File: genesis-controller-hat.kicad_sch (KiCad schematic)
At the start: 1 part, among them J1 GPIO

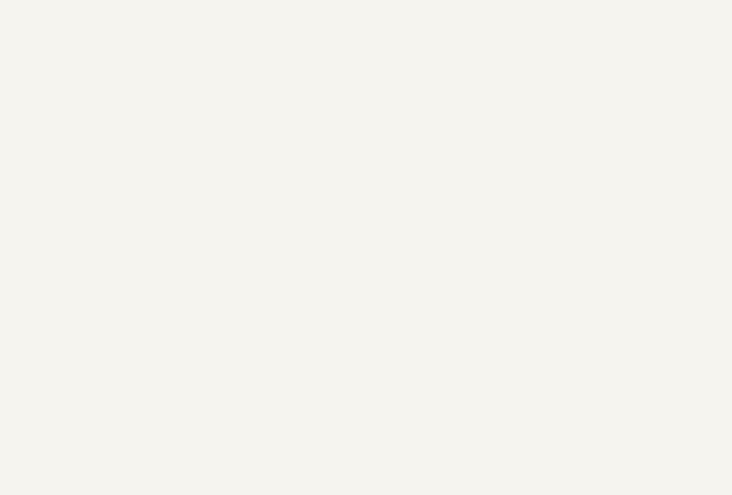
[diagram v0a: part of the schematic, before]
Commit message: Wire Player 1 DB9 connector (J2) to the GPIO header
Up/Down/Left/Right/TL/SELECT/TR land on GPIO5/6/7/9/4/10 respectively per
sega_board.h; +3.3V and GND are local power symbols that merge onto the
header's existing +3.3V/GND nets by KiCad's global-power-symbol naming
rule, and the shell/mounting pad is explicitly marked no-connect per the
approved no-extra-protection design.

Co-Authored-By: Claude Sonnet 5 <noreply@anthropic.com>
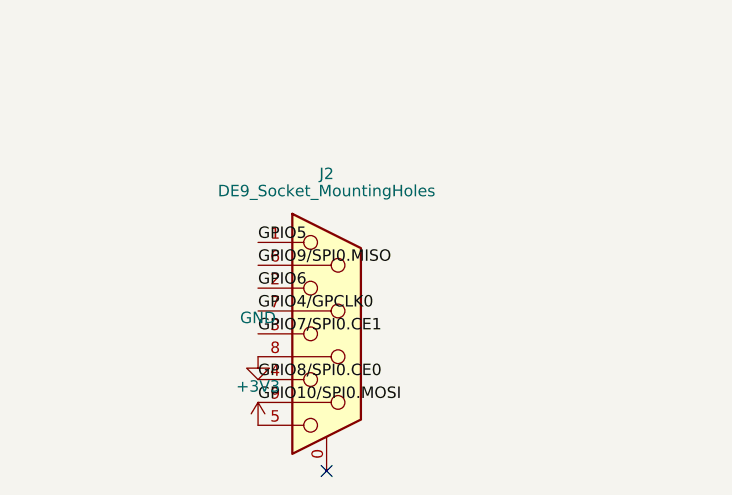
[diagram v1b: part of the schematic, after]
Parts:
- added J2: DE9_Socket_MountingHoles, Connector_Dsub:DSUB-9_Socket_Vertical_P2.77x2.84mm_MountingHoles, symbol Connector:DE9_Socket_MountingHoles
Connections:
- net +3V3: now also J2.5
- net GND: now also J2.8
- net GPIO10/SPI0.MOSI: now also J2.9
- net GPIO4/GPCLK0: now also J2.7
- net GPIO5: now also J2.1
- net GPIO6: now also J2.2
- net GPIO7/SPI0.CE1: now also J2.3
- net GPIO8/SPI0.CE0: now also J2.4
- net GPIO9/SPI0.MISO: now also J2.6
- no-connect marks 14 -> 15
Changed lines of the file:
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@@
 		(at 73.66 76.2)
 	)
+	(symbol
+		(lib_id "Connector:DE9_Socket_MountingHoles")
+		(at 50.8 254.0 0)
+		(unit 1)
+		(exclude_from_sim no)
+		(in_bom yes)
+		(on_board yes)
+		(dnp no)
+		(property "Reference" "J2"
+			(at 50.8 236.22 0)
+			(effects
+				(font
+					(size 1.27 1.27)
+				)
+			)
+		)
+		(property "Value" "DE9_Socket_MountingHoles"
+			(at 50.8 238.125 0)
+			(effects
+				(font
+					(size 1.27 1.27)
+				)
+			)
+		)
+		(property "Footprint" "Connector_Dsub:DSUB-9_Socket_Vertical_P2.77x2.84mm_MountingHoles"
+			(at 50.8 254.0 0)
+			(effects
+				(font
+					(size 1.27 1.27)
+				)
+				(hide yes)
+			)
+		)
+		(property "Datasheet" "~"
+			(at 50.8 254.0 0)
+			(effects
+				(font
+					(size 1.27 1.27)
+				)
+				(hide yes)
+			)
+		)
+		(instances
+			(project "RaspberryPi-HAT"
+				(path "/e63e39d7-6ac0-4ffd-8aa3-1841a4541b55"
+					(reference "J2")
+					(unit 1)
+				)
+			)
+		)
+	)
+	(label "GPIO5"
+		(at 43.18 243.84 180)
+		(effects
+			(font
+				(size 1.27 1.27)
+			)
+			(justify left bottom)
+		)
+	)
+	(label "GPIO6"
+		(at 43.18 248.92 180)
+		(effects
+			(font
+				(size 1.27 1.27)
+			)
+			(justify left bottom)
+		)
+	)
+	(label "GPIO7{slash}SPI0.CE1"
+		(at 43.18 254.0 180)
+		(effects
+			(font
+				(size 1.27 1.27)
+			)
+			(justify left bottom)
+		)
+	)
+	(label "GPIO8{slash}SPI0.CE0"
+		(at 43.18 259.08 180)
+		(effects
+			(font
+				(size 1.27 1.27)
+			)
+			(justify left bottom)
+		)
+	)
+	(label "GPIO9{slash}SPI0.MISO"
+		(at 43.18 246.38 180)
+		(effects
+			(font
+				(size 1.27 1.27)
+			)
+			(justify left bottom)
+		)
+	)
+	(label "GPIO4{slash}GPCLK0"
+		(at 43.18 251.46 180)
+		(effects
+			(font
+				(size 1.27 1.27)
+			)
+			(justify left bottom)
+		)
+	)
+	(label "GPIO10{slash}SPI0.MOSI"
+		(at 43.18 261.62 180)
+		(effects
+			(font
+				(size 1.27 1.27)
+			)
+			(justify left bottom)
+		)
+	)
+	(symbol
+		(lib_id "power:+3.3V")
+		(at 43.18 264.16 0)
+		(unit 1)
+		(exclude_from_sim no)
+		(in_bom yes)
+		(on_board yes)
+		(dnp no)
+		(property "Reference" "#PWR901"
+			(at 43.18 267.97 0)
+			(effects
+				(font
+					(size 1.27 1.27)
+				)
+				(hide yes)
+			)
+		)
+		(property "Value" "+3V3"
+			(at 43.18 259.84000000000003 0)
+			(effects
+				(font
+					(size 1.27 1.27)
+				)
+			)
+		)
+		(property "Footprint" ""
+			(at 43.18 264.16 0)
+			(effects
+				(font
+					(size 1.27 1.27)
+				)
+			)
+		)
+		(property "Datasheet" ""
+			(at 43.18 264.16 0)
+			(effects
+				(font
+					(size 1.27 1.27)
+				)
+			)
+		)
+		(pin "1"
+		)
+		(instances
+			(project "RaspberryPi-HAT"
+				(path "/e63e39d7-6ac0-4ffd-8aa3-1841a4541b55"
+					(reference "#PWR901")
+					(unit 1)
+				)
+			)
+		)
+	)
+	(symbol
+		(lib_id "power:GND")
+		(at 43.18 256.54 0)
+		(unit 1)
+		(exclude_from_sim no)
+		(in_bom yes)
+		(on_board yes)
+		(dnp no)
+		(property "Reference" "#PWR902"
+			(at 43.18 260.35 0)
+			(effects
+				(font
+					(size 1.27 1.27)
+				)
+				(hide yes)
+			)
+		)
+		(property "Value" "GND"
+			(at 43.18 252.22000000000003 0)
+			(effects
+				(font
+					(size 1.27 1.27)
+				)
+			)
+		)
+		(property "Footprint" ""
+			(at 43.18 256.54 0)
+			(effects
+				(font
+					(size 1.27 1.27)
+				)
+			)
+		)
+		(property "Datasheet" ""
+			(at 43.18 256.54 0)
+			(effects
+				(font
+					(size 1.27 1.27)
+				)
+			)
+		)
+		(pin "1"
+		)
+		(instances
+			(project "RaspberryPi-HAT"
+				(path "/e63e39d7-6ac0-4ffd-8aa3-1841a4541b55"
+					(reference "#PWR902")
+					(unit 1)
+				)
+			)
+		)
+	)
+	(no_connect
+		(at 50.8 269.24)
+	)
 )

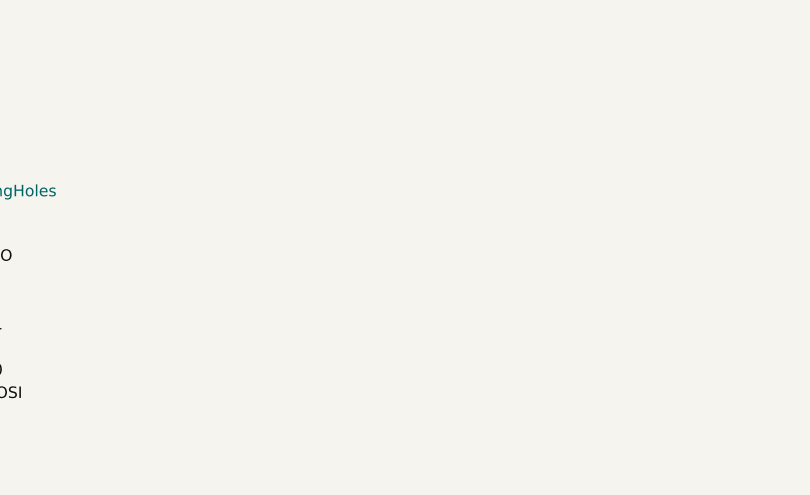
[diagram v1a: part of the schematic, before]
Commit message: Wire Player 2 DB9 connector (J3) to the GPIO header
Mirrors Task 4's Player 1 wiring onto GPIO12/13/16/17/22/11/23 per
sega_board.h. Schematic ERC is now fully clean (0 errors, 0 warnings).

Co-Authored-By: Claude Sonnet 5 <noreply@anthropic.com>
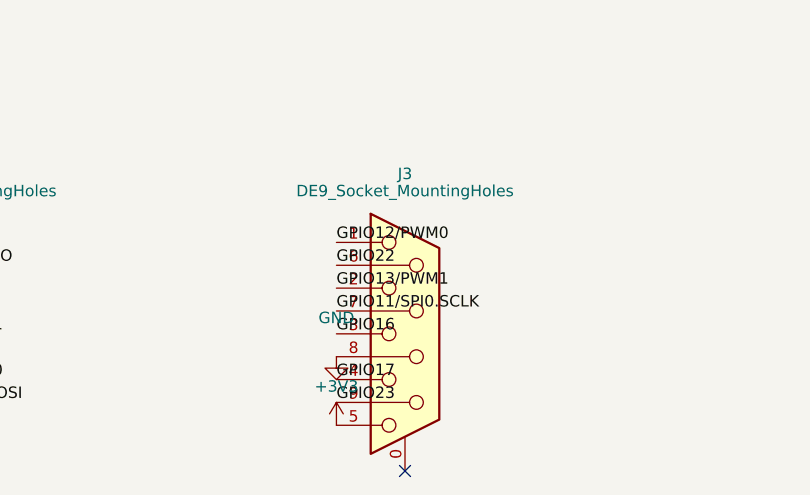
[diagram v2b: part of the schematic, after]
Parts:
- added J3: DE9_Socket_MountingHoles, Connector_Dsub:DSUB-9_Socket_Vertical_P2.77x2.84mm_MountingHoles, symbol Connector:DE9_Socket_MountingHoles
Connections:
- net +3V3: now also J3.5
- net GND: now also J3.8
- net GPIO11/SPI0.SCLK: now also J3.7
- net GPIO12/PWM0: now also J3.1
- net GPIO13/PWM1: now also J3.2
- net GPIO16: now also J3.3
- net GPIO17: now also J3.4
- net GPIO22: now also J3.6
- net GPIO23: now also J3.9
- no-connect marks 15 -> 16
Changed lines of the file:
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@@
 		(at 50.8 269.24)
 	)
+	(symbol
+		(lib_id "Connector:DE9_Socket_MountingHoles")
+		(at 101.6 254.0 0)
+		(unit 1)
+		(exclude_from_sim no)
+		(in_bom yes)
+		(on_board yes)
+		(dnp no)
+		(property "Reference" "J3"
+			(at 101.6 236.22 0)
+			(effects
+				(font
+					(size 1.27 1.27)
+				)
+			)
+		)
+		(property "Value" "DE9_Socket_MountingHoles"
+			(at 101.6 238.125 0)
+			(effects
+				(font
+					(size 1.27 1.27)
+				)
+			)
+		)
+		(property "Footprint" "Connector_Dsub:DSUB-9_Socket_Vertical_P2.77x2.84mm_MountingHoles"
+			(at 101.6 254.0 0)
+			(effects
+				(font
+					(size 1.27 1.27)
+				)
+				(hide yes)
+			)
+		)
+		(property "Datasheet" "~"
+			(at 101.6 254.0 0)
+			(effects
+				(font
+					(size 1.27 1.27)
+				)
+				(hide yes)
+			)
+		)
+		(instances
+			(project "RaspberryPi-HAT"
+				(path "/e63e39d7-6ac0-4ffd-8aa3-1841a4541b55"
+					(reference "J3")
+					(unit 1)
+				)
+			)
+		)
+	)
+	(label "GPIO12{slash}PWM0"
+		(at 93.98 243.84 180)
+		(effects
+			(font
+				(size 1.27 1.27)
+			)
+			(justify left bottom)
+		)
+	)
+	(label "GPIO13{slash}PWM1"
+		(at 93.98 248.92 180)
+		(effects
+			(font
+				(size 1.27 1.27)
+			)
+			(justify left bottom)
+		)
+	)
+	(label "GPIO16"
+		(at 93.98 254.0 180)
+		(effects
+			(font
+				(size 1.27 1.27)
+			)
+			(justify left bottom)
+		)
+	)
+	(label "GPIO17"
+		(at 93.98 259.08 180)
+		(effects
+			(font
+				(size 1.27 1.27)
+			)
+			(justify left bottom)
+		)
+	)
+	(label "GPIO22"
+		(at 93.98 246.38 180)
+		(effects
+			(font
+				(size 1.27 1.27)
+			)
+			(justify left bottom)
+		)
+	)
+	(label "GPIO11{slash}SPI0.SCLK"
+		(at 93.98 251.46 180)
+		(effects
+			(font
+				(size 1.27 1.27)
+			)
+			(justify left bottom)
+		)
+	)
+	(label "GPIO23"
+		(at 93.98 261.62 180)
+		(effects
+			(font
+				(size 1.27 1.27)
+			)
+			(justify left bottom)
+		)
+	)
+	(symbol
+		(lib_id "power:+3.3V")
+		(at 93.98 264.16 0)
+		(unit 1)
+		(exclude_from_sim no)
+		(in_bom yes)
+		(on_board yes)
+		(dnp no)
+		(property "Reference" "#PWR903"
+			(at 93.98 267.97 0)
+			(effects
+				(font
+					(size 1.27 1.27)
+				)
+				(hide yes)
+			)
+		)
+		(property "Value" "+3V3"
+			(at 93.98 259.84000000000003 0)
+			(effects
+				(font
+					(size 1.27 1.27)
+				)
+			)
+		)
+		(property "Footprint" ""
+			(at 93.98 264.16 0)
+			(effects
+				(font
+					(size 1.27 1.27)
+				)
+			)
+		)
+		(property "Datasheet" ""
+			(at 93.98 264.16 0)
+			(effects
+				(font
+					(size 1.27 1.27)
+				)
+			)
+		)
+		(pin "1"
+		)
+		(instances
+			(project "RaspberryPi-HAT"
+				(path "/e63e39d7-6ac0-4ffd-8aa3-1841a4541b55"
+					(reference "#PWR903")
+					(unit 1)
+				)
+			)
+		)
+	)
+	(symbol
+		(lib_id "power:GND")
+		(at 93.98 256.54 0)
+		(unit 1)
+		(exclude_from_sim no)
+		(in_bom yes)
+		(on_board yes)
+		(dnp no)
+		(property "Reference" "#PWR904"
+			(at 93.98 260.35 0)
+			(effects
+				(font
+					(size 1.27 1.27)
+				)
+				(hide yes)
+			)
+		)
+		(property "Value" "GND"
+			(at 93.98 252.22000000000003 0)
+			(effects
+				(font
+					(size 1.27 1.27)
+				)
+			)
+		)
+		(property "Footprint" ""
+			(at 93.98 256.54 0)
+			(effects
+				(font
+					(size 1.27 1.27)
+				)
+			)
+		)
+		(property "Datasheet" ""
+			(at 93.98 256.54 0)
+			(effects
+				(font
+					(size 1.27 1.27)
+				)
+			)
+		)
+		(pin "1"
+		)
+		(instances
+			(project "RaspberryPi-HAT"
+				(path "/e63e39d7-6ac0-4ffd-8aa3-1841a4541b55"
+					(reference "#PWR904")
+					(unit 1)
+				)
+			)
+		)
+	)
+	(no_connect
+		(at 101.6 269.24)
+	)
 )

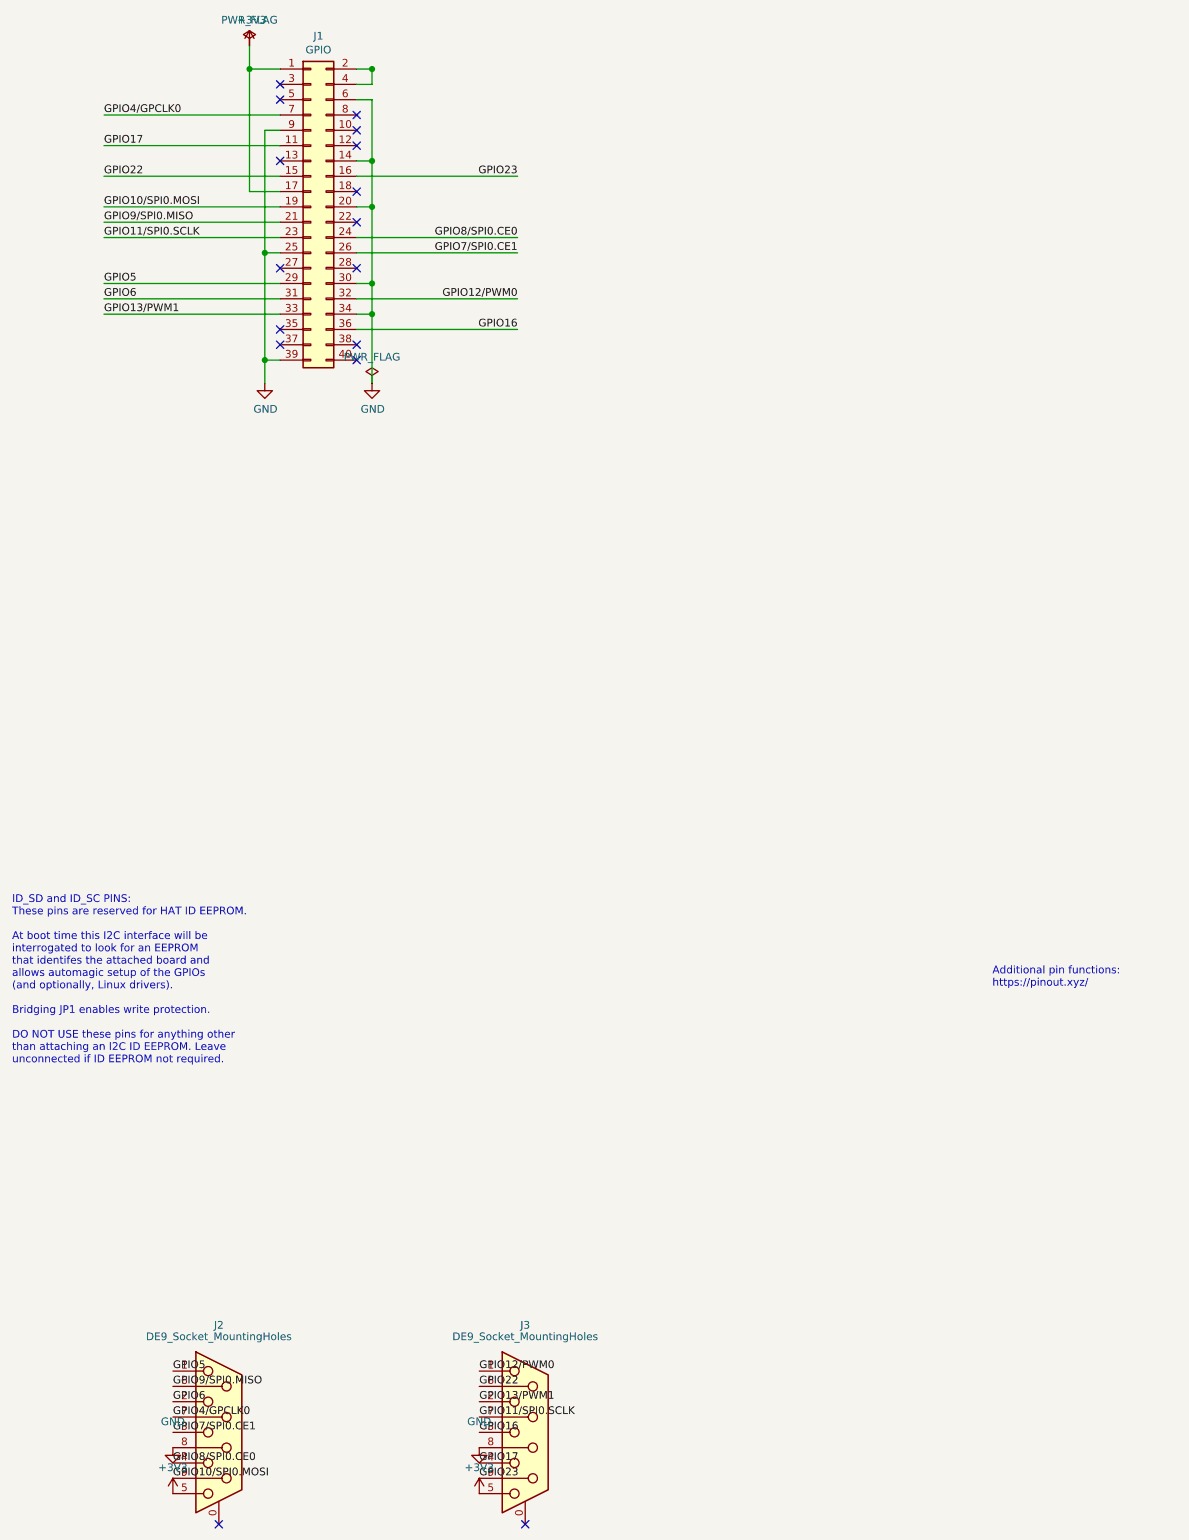
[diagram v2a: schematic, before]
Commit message: Reassign GPIO pin map to eliminate PCB routing crossings
Rewires J2/J3 to the new pin assignment (Port 1 select=22 data=10,23,27,17,24,4;
Port 2 select=12 data=26,13,6,5,16,7) that groups each port's signals onto
physically adjacent GPIO header columns nearest that port's connector. This
lets the board route with zero same-layer trace crossings and zero
hole-clearance violations (was 14 tracks_crossing + 4 hole_clearance),
reducing total DRC violations from 30 errors/6 warnings to 16/6. ERC remains
0/0, and the schematic wiring matches the firmware repo's updated
sega_board.h exactly (verified via scripts/check_pinmap.py).

See docs/reviews/2026-07-22-pinmap-reassignment.md for the full root-cause
analysis and before/after DRC breakdown.

Co-Authored-By: Claude Sonnet 5 <noreply@anthropic.com>
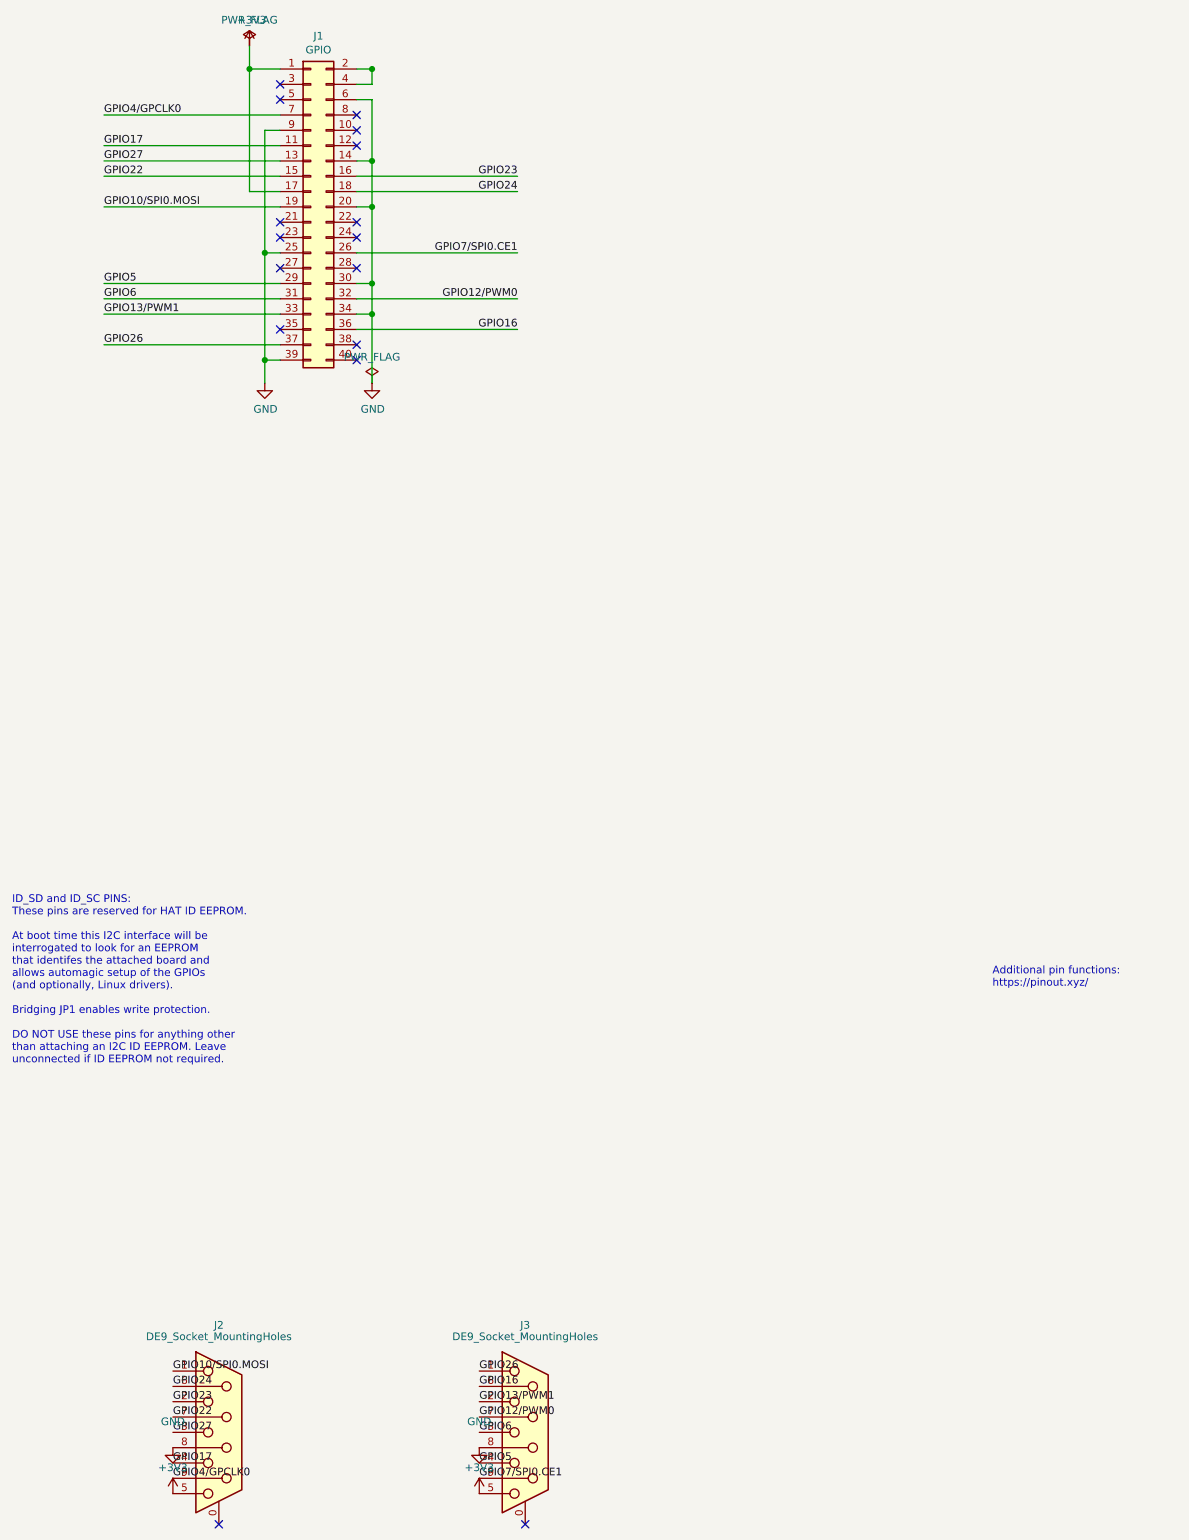
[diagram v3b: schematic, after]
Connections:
- net GPIO10/SPI0.MOSI: now also J2.1; no longer J2.9
- net GPIO12/PWM0: now also J3.7; no longer J3.1
- net GPIO16: now also J3.6; no longer J3.3
- net GPIO17: now also J2.4; no longer J3.4
- net GPIO22: now also J2.7; no longer J3.6
- net GPIO23: now also J2.2; no longer J3.9
- net GPIO4/GPCLK0: now also J2.9; no longer J2.7
- net GPIO5: now also J3.4; no longer J2.1
- net GPIO6: now also J3.3; no longer J2.2
- net GPIO7/SPI0.CE1: now also J3.9; no longer J2.3
- net GPIO27: now reaches J1.13 (Pin_13)
- net GPIO27: now also J2.3
- net GPIO24: now reaches J1.18 (Pin_18)
- net GPIO24: now also J2.6
- net GPIO26: now reaches J1.37 (Pin_37)
- net GPIO26: now also J3.1
- net GPIO11/SPI0.SCLK: no longer names the net of J1.23 (Pin_23)
- net GPIO11/SPI0.SCLK: no longer J3.7
- net GPIO8/SPI0.CE0: no longer names the net of J1.24 (Pin_24)
- net GPIO8/SPI0.CE0: no longer J2.4
- net GPIO9/SPI0.MISO: no longer names the net of J1.21 (Pin_21)
- net GPIO9/SPI0.MISO: no longer J2.6
